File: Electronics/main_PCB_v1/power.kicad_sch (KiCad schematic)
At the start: 36 parts, among them J301 Conn_01x02, J305 Conn_01x02, J306 Conn_01x02, J307 Conn_01x02, J308 Conn_01x02, J309 Conn_01x02, J310 Conn_01x02, Q302 DMP3028LFDE, T301 NVMFS4C05NT1G, T302 NVMFS4C05NT1G, U301 LMR43620MB5RPER, U302 LMR43620MB5RPER

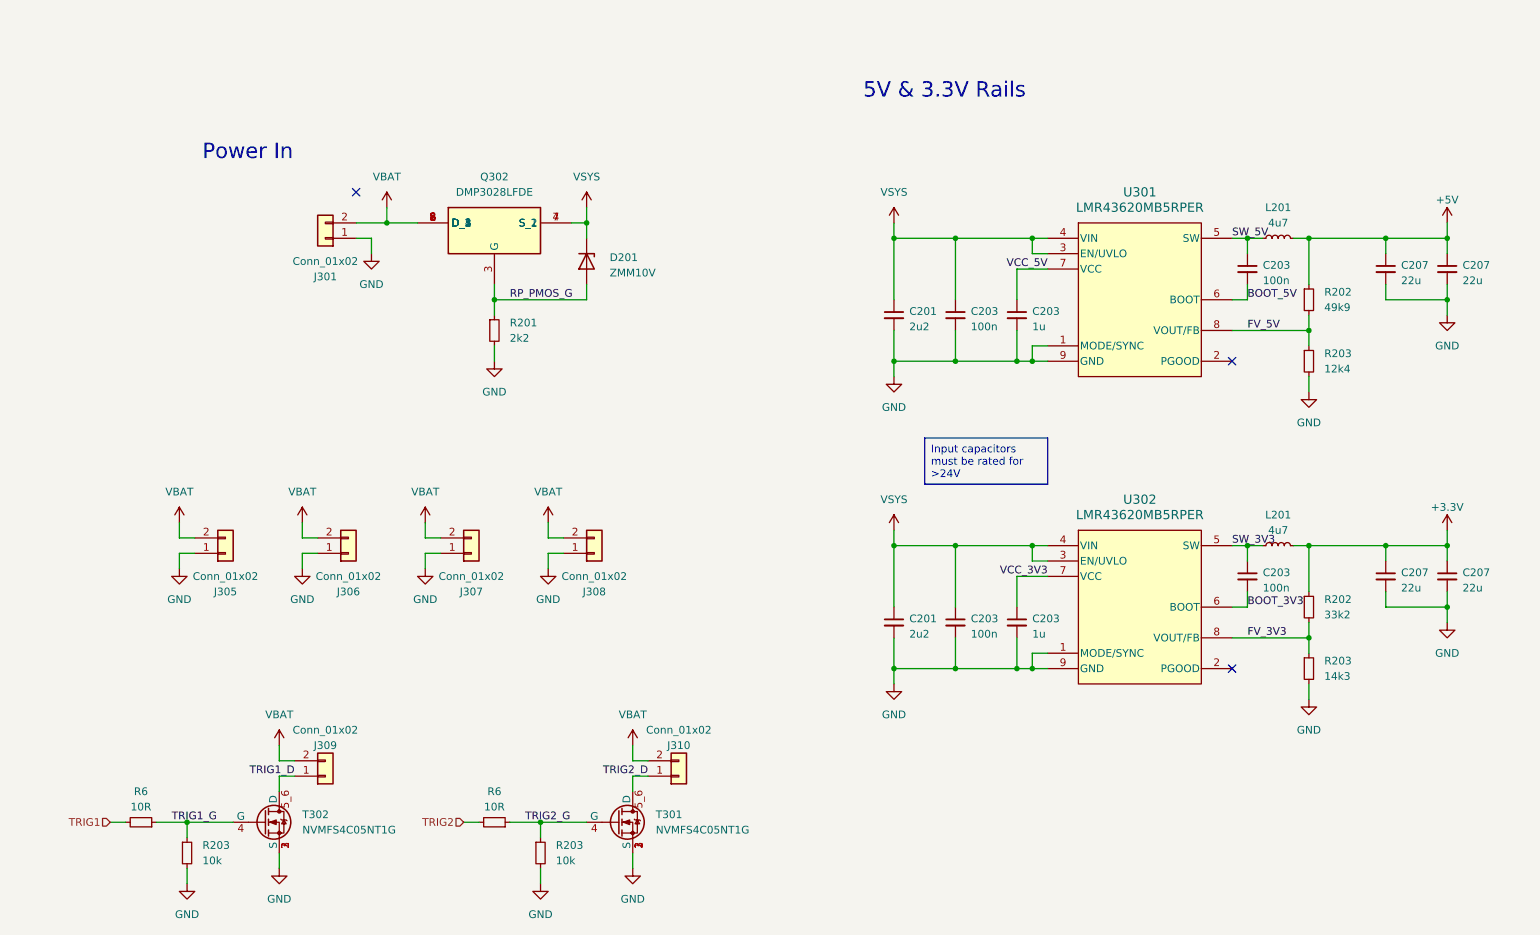
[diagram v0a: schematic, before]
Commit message: Added 12V rail to PCB
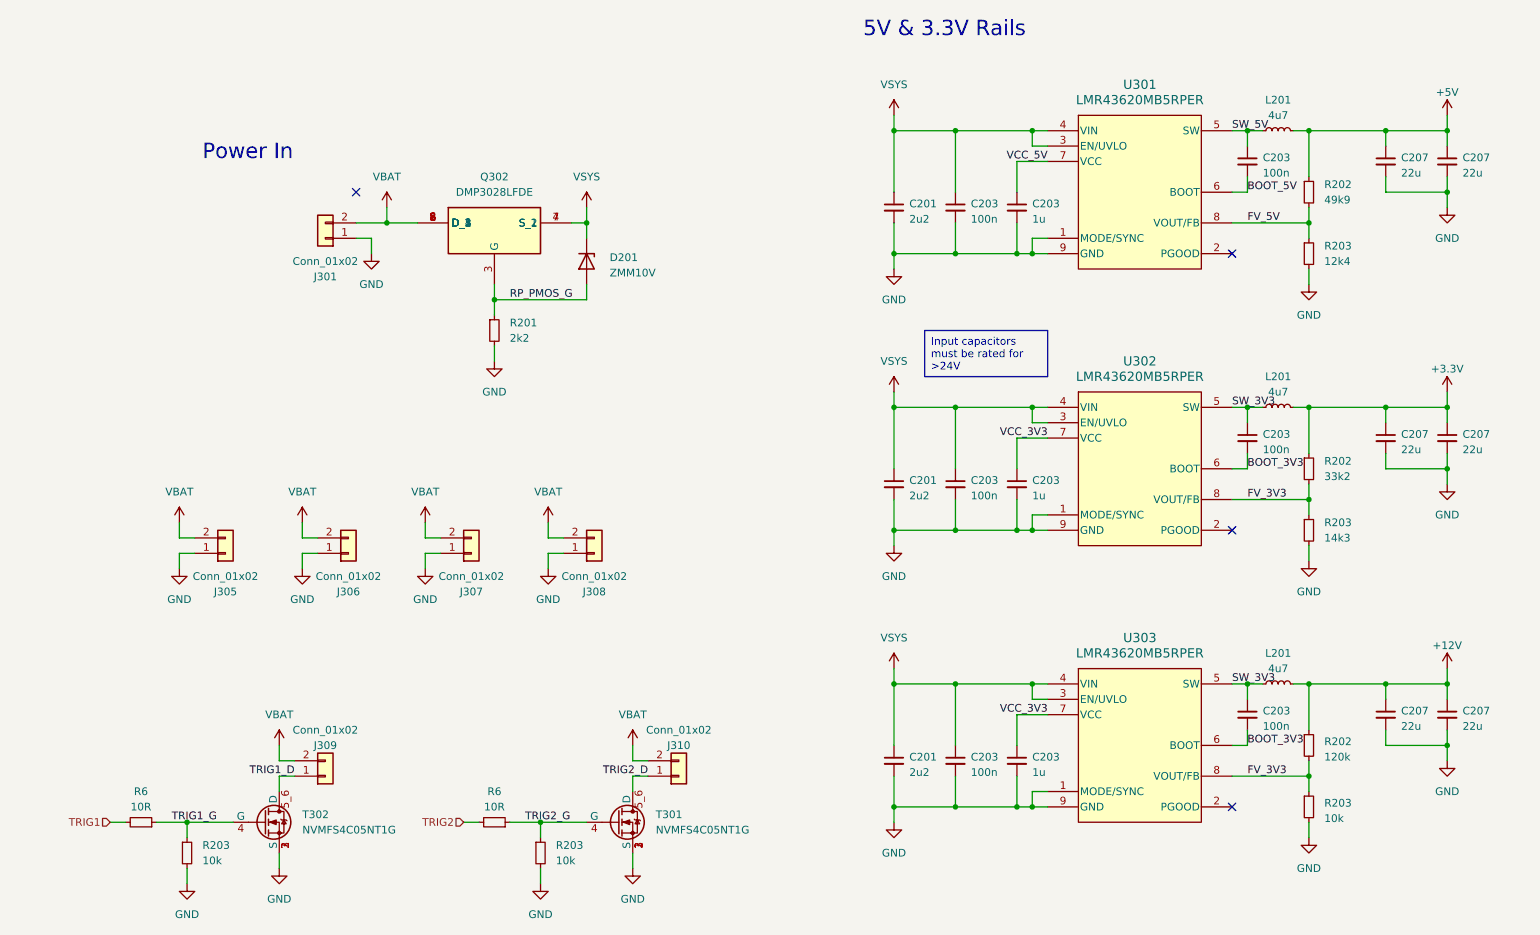
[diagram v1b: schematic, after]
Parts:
- added C201: 2u2, Capacitor_SMD:C_0603_1608Metric, symbol Device:C_Small
- added C203 (x2): 100n, Capacitor_SMD:C_0402_1005Metric, symbol Device:C_Small
- added C203: 1u, Capacitor_SMD:C_0402_1005Metric, symbol Device:C_Small
- added C207 (x2): 22u, Capacitor_SMD:C_0603_1608Metric, symbol Device:C_Small
- added L201: 4u7, Inductor_SMD:L_Chilisin_BMRA00040420, symbol Device:L_Small
- added R202: 120k, Resistor_SMD:R_0402_1005Metric, symbol Device:R_Small
- added R203: 10k, Resistor_SMD:R_0402_1005Metric, symbol Device:R_Small
- added U303: LMR43620MB5RPER, SSL Footprints:LMR43620MB5RPER_TEX, symbol LMR43620MB5RPER:LMR43620MB5RPER
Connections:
- net BOOT_3V3: now also C203.2, U303.6 (BOOT)
- net FV_3V3: now also R202.2, R203.1, U303.8 (VOUT/FB)
- net GND: now also C201.2, C203.2, C203.2, C207.2, C207.2, R203.2, U303.1 (MODE/SYNC), U303.9 (GND)
- net SW_3V3: now also C203.1, L201.1, U303.5 (SW)
- net VCC_3V3: now also C203.1, U303.7 (VCC)
- net VSYS: now also C201.1, C203.1, U303.3 (EN/UVLO), U303.4 (VIN)
- new net +12V: C207.1, C207.1, L201.2, R202.1
- no-connect marks 3 -> 4
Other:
- moved on the sheet: C201, C203, C207, L201, R202, R203, U301, U302

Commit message: PCB Finished
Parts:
- added C203 (x3): 1n, Capacitor_SMD:C_0402_1005Metric, symbol Device:C_Small
- added C203 (x3): 100p, Capacitor_SMD:C_0402_1005Metric, symbol Device:C_Small
- added D302 (x3): Green, LED_SMD:LED_0603_1608Metric, symbol Device:LED_Small
- added J302: Conn_01x02, Connector_AMASS:AMASS_XT30U-F_1x02_P5.0mm_Vertical, symbol Connector_Generic:Conn_01x02
- added R23: 22k, Resistor_SMD:R_0402_1005Metric, symbol Device:R_Small
- added R23: 3k3, Resistor_SMD:R_0402_1005Metric, symbol Device:R_Small
- added R23: 6k8, Resistor_SMD:R_0402_1005Metric, symbol Device:R_Small
- R202: value 33k2 -> 33k
- R203: value 12k4 -> 10k
- R203: value 14k3 -> 10k
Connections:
- net +12V: now also C203.1, D302.2 (A), J302.2 (Pin_2)
- net +3.3V: now also C203.1, D302.2 (A)
- net +5V: now also C203.1, D302.2 (A)
- net BOOT_3V3: no longer C203.2, U303.6 (BOOT)
- net FV_3V3: now also C203.1, C203.2; no longer R202.2, R203.1, U303.8 (VOUT/FB)
- net FV_5V: now also C203.1, C203.2
- net GND: now also C203.2, C203.2, C203.2, J302.1 (Pin_1), R23.1, R23.1, R23.1
- net SW_3V3: no longer C203.1, L201.1, U303.5 (SW)
- net VCC_3V3: no longer C203.1, U303.7 (VCC)
- new net BOOT_12V: C203.2, U303.6 (BOOT)
- new net FV_12V: C203.1, C203.2, R202.2, R203.1, U303.8 (VOUT/FB)
- new net LED12V: D302.1 (K), R23.2
- new net LED3V3: D302.1 (K), R23.2
- new net LED5V: D302.1 (K), R23.2
- new net SW_12V: C203.1, L201.1, U303.5 (SW)
- new net VCC_12V: C203.1, U303.7 (VCC)
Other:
- moved on the sheet: C201, C203, C207, D201, J301, J305, J306, J307, J308, J309, J310, L201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

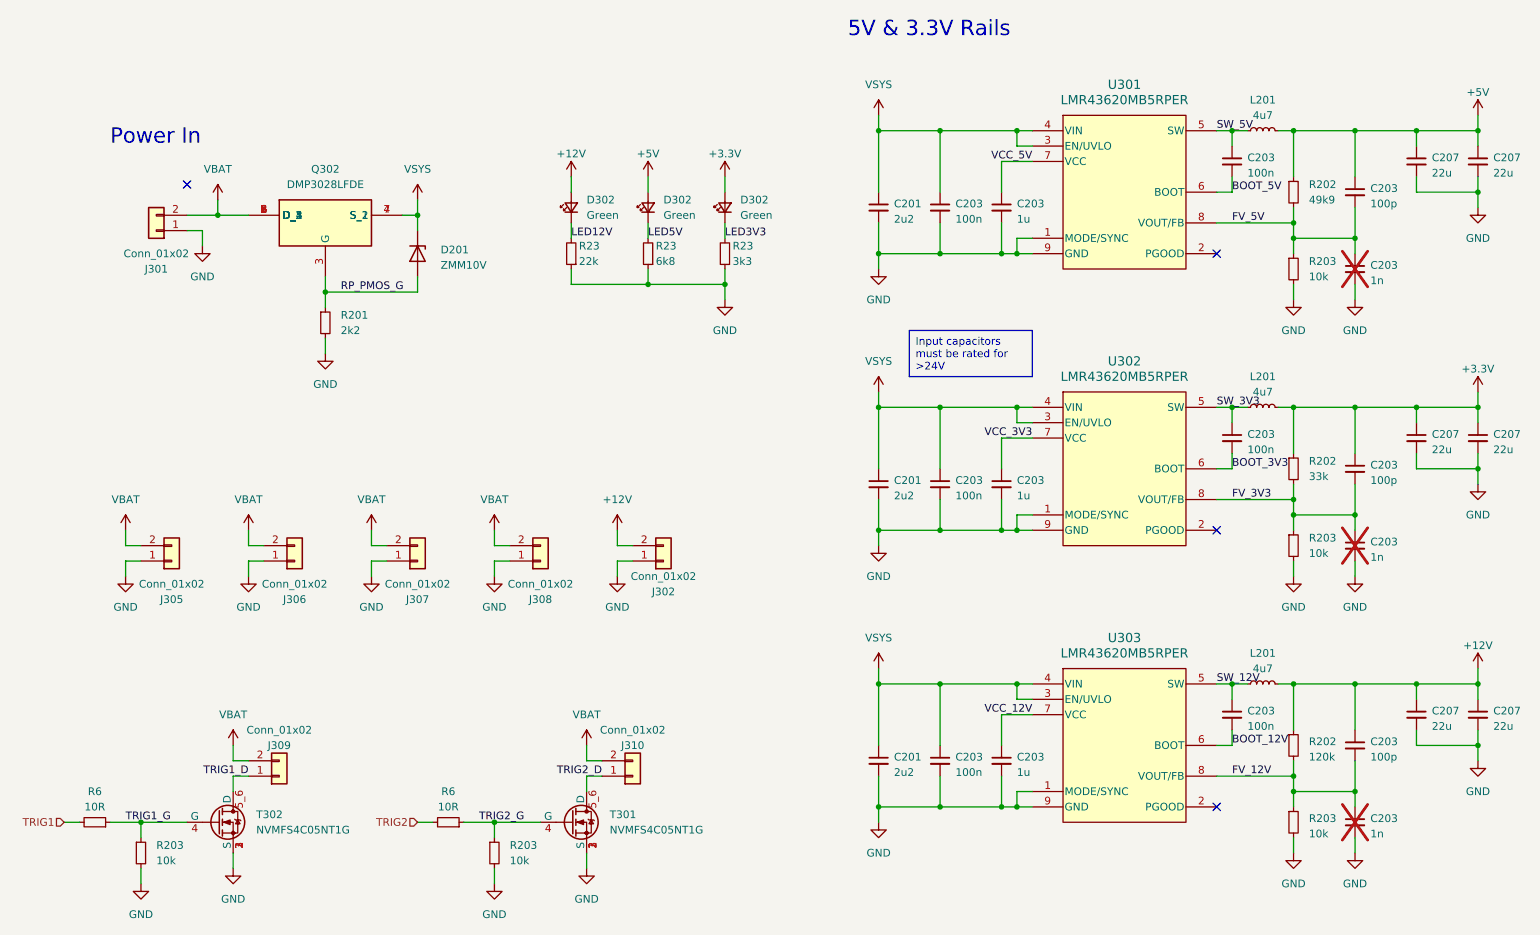
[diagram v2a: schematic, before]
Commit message: Updated buck feedback values
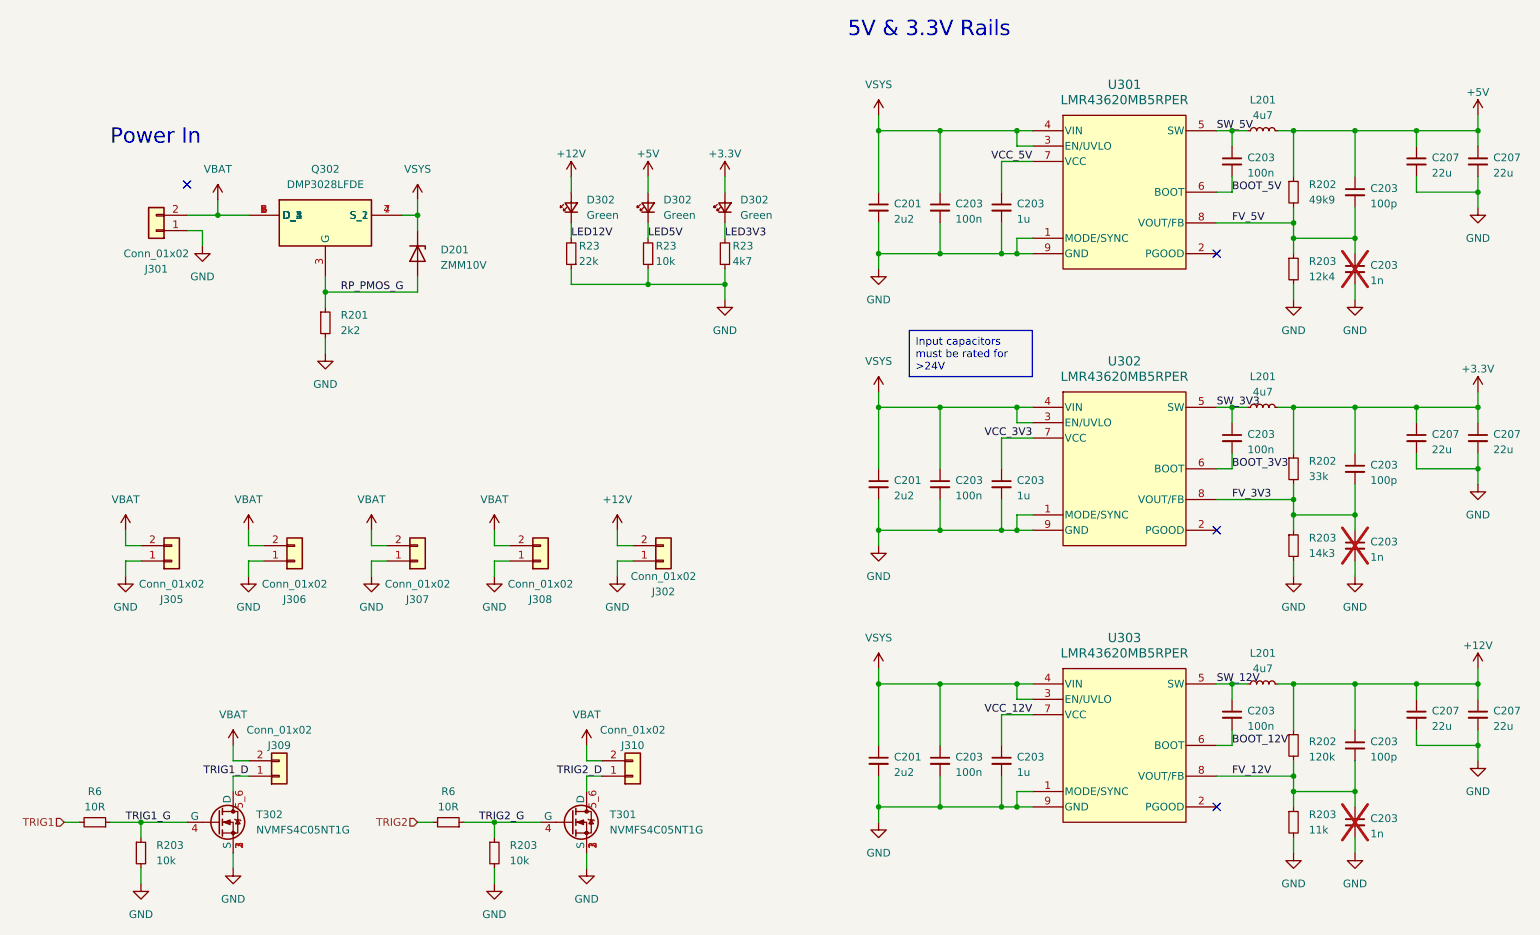
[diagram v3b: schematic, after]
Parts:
- R203: value 10k -> 12k4
- R203: value 10k -> 11k
- R203: value 10k -> 14k3
- R23: value 3k3 -> 4k7
- R23: value 6k8 -> 10k
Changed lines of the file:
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@@
       (effects (font (size 1.27 1.27)) (justify left))
     )
-    (property "Value" "10k" (at 231.14 59.69 0)
+    (property "Value" "12k4" (at 231.14 59.69 0)
       (effects (font (size 1.27 1.27)) (justify left))
     )
@@
   (symbol (lib_id "Device:R_Small") (at 228.6 149.86 0) (unit 1)
     (in_bom yes) (on_board yes) (dnp no) (fields_autoplaced)
-    (property "Reference" "R203" (at 231.14 149.225 0)
-      (effects (font (size 1.27 1.27)) (justify left))
-    )
-    (property "Value" "10k" (at 231.14 151.765 0)
+    (property "Reference" "R203" (at 231.14 148.59 0)
+      (effects (font (size 1.27 1.27)) (justify left))
+    )
+    (property "Value" "11k" (at 231.14 151.13 0)
       (effects (font (size 1.27 1.27)) (justify left))
     )
@@
       (effects (font (size 1.27 1.27)) (justify right))
     )
-    (property "Value" "3k3" (at 135.89 57.15 0)
+    (property "Value" "4k7" (at 135.89 57.15 0)
       (effects (font (size 1.27 1.27)) (justify right))
     )
@@
       (effects (font (size 1.27 1.27)) (justify left))
     )
-    (property "Value" "10k" (at 231.14 105.41 0)
+    (property "Value" "14k3" (at 231.14 105.41 0)
       (effects (font (size 1.27 1.27)) (justify left))
     )
@@
       (effects (font (size 1.27 1.27)) (justify right))
     )
-    (property "Value" "6k8" (at 123.19 57.15 0)
+    (property "Value" "10k" (at 123.19 57.15 0)
       (effects (font (size 1.27 1.27)) (justify right))
     )
